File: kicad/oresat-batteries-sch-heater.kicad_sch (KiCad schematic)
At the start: 20 parts, among them Q20 PMV45EN, Q21 PMV45EN, Q38 PMV45EN, Q39 PMV45EN, Q42 MOSFET-PCH-SOT23-6, Q43 MOSFET-PCH-SOT23-6

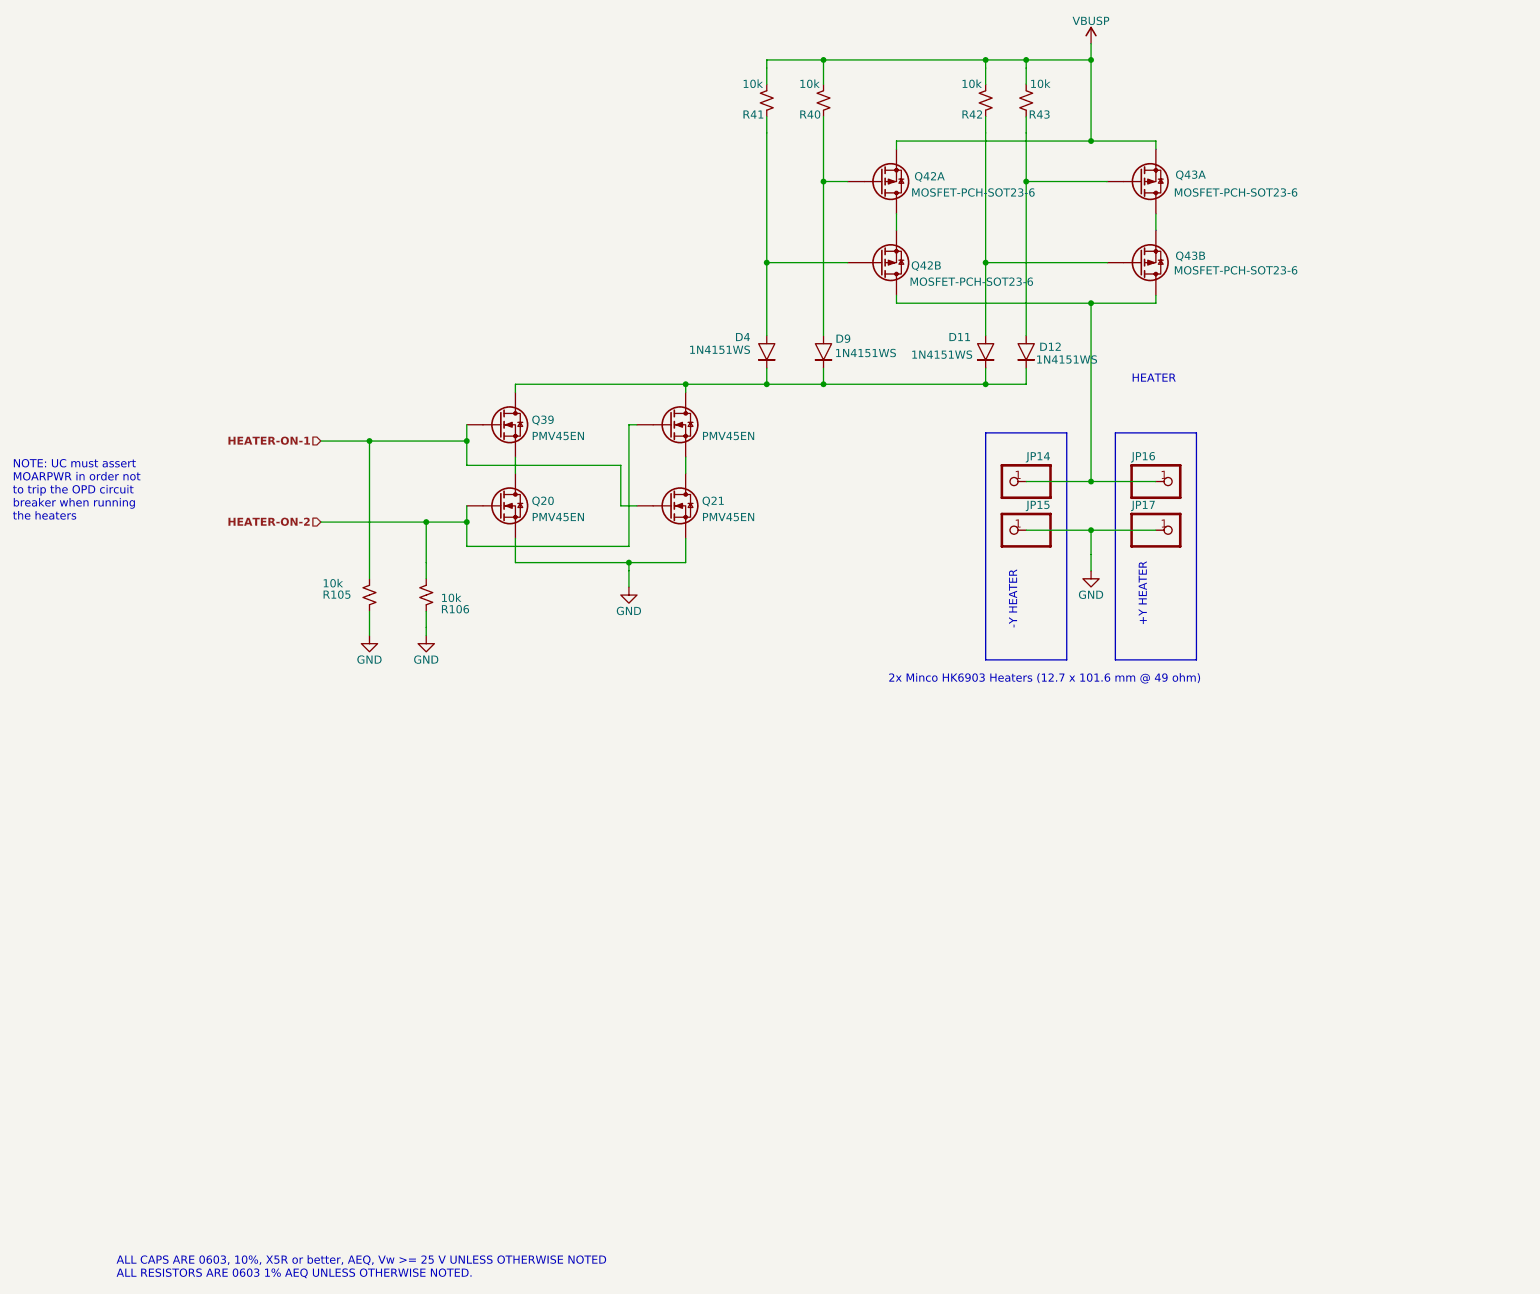
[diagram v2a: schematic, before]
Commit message: Progress on battery card v4
Moved in -batt cutoffs, which caused a lot of pain and suffering. Started updating BOM, and fixed all transistor packages. Updated resistor packages, too. Still needs a lot of cleanup, but probably 80% done now.
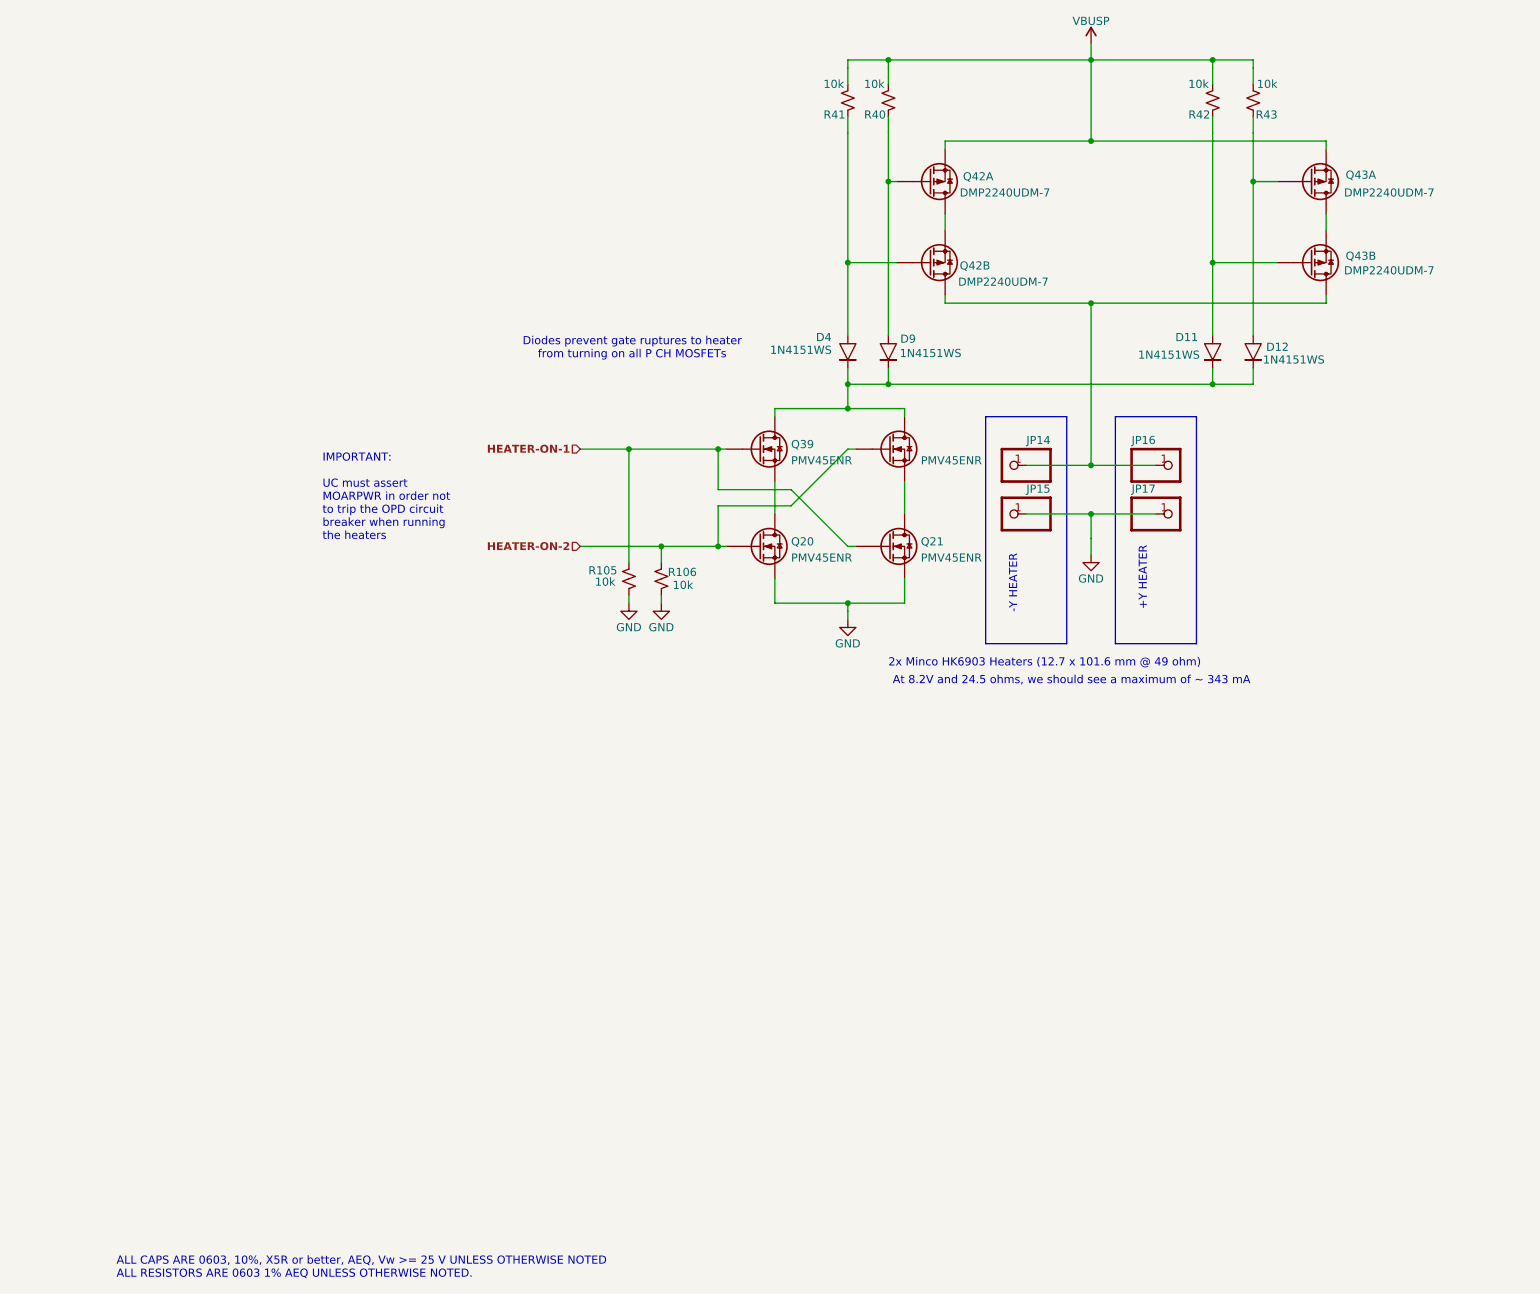
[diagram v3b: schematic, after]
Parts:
- Q20, Q21, Q38, Q39: value PMV45EN -> PMV45ENR; footprint oresat-batteries:SOT23-3 -> Package_TO_SOT_SMD:SOT-23; DIS (none) -> DigiKey; DPN (none) -> 1727-2307-1-ND; MFR (none) -> Nexperia; MPN (none) -> PMV45EN2R
- Q42, Q43: value MOSFET-PCH-SOT23-6 -> DMP2240UDM-7; footprint oresat-batteries:SOT23-6 -> Package_TO_SOT_SMD:SOT-23-6; DIS (none) -> DigiKey; DPN (none) -> DMP2240UDMDICT-ND; MFR (none) -> Diodes Incorporated; MPN (none) -> DMP2240UDM-7
- R105, R106, R40, R41, R42, R43: footprint oresat-batteries:.0603-C-NOSILK -> oresat-passives:0603-C-NOSILK
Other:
- note added: "At 8.2V and 24.5 ohms, we should see a maximum of ~ 343 mA"
- note added: "Diodes prevent gate ruptures to heater from turning on all P CH MOSFETs"
- note added: "IMPORTANT: UC must assert MOARPWR in order not to trip the OPD circuit breaker when running the heaters"
- note removed: "HEATER"
- note removed: "NOTE: UC must assert MOARPWR in order not to trip the OPD circuit breaker when running the heaters~{}"
- moved on the sheet: D11, D12, D4, D9, JP14, JP15, JP16, JP17, Q20, Q21, Q39, Q42A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

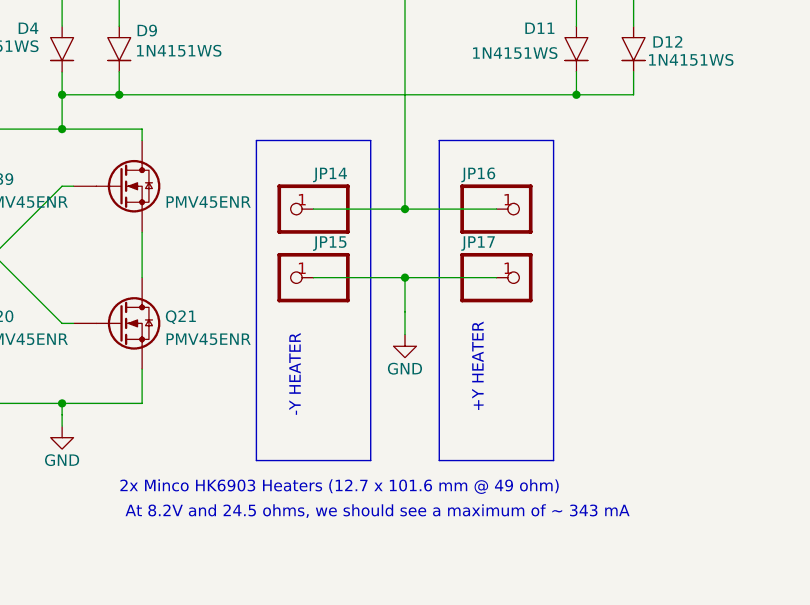
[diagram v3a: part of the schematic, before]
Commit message: Updated BOM, ready for polish and switch to MCXN
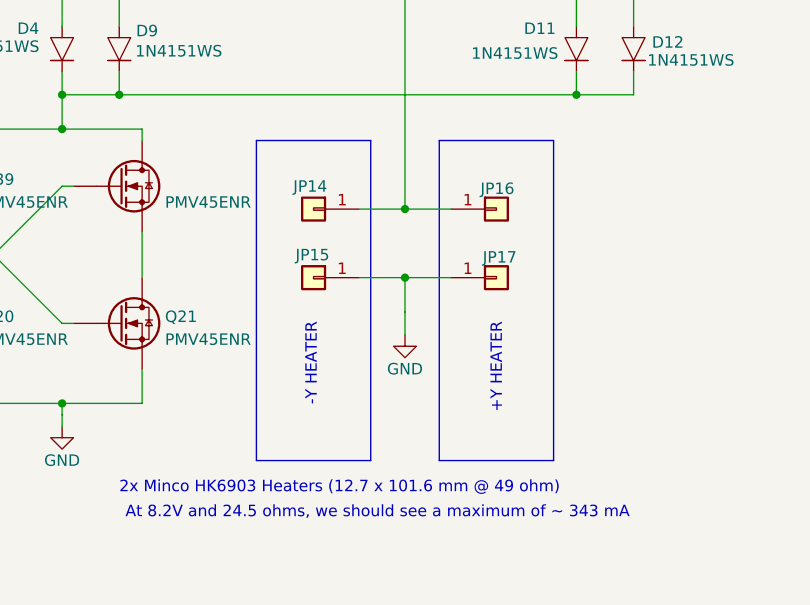
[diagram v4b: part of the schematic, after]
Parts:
- JP14, JP15, JP16, JP17: footprint oresat-batteries:1X01 -> Connector_PinHeader_2.54mm:PinHeader_1x01_P2.54mm_Vertical; symbol oresat-batteries-eagle-import:PINHD-1X1 -> Connector_Generic:Conn_01x01
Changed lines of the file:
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@@
 	(text "+Y HEATER"
 		(exclude_from_sim no)
-		(at 274.32 151.13 90)
+		(at 276.352 151.13 90)
 		(effects
 			(font
@@
 	(text "-Y HEATER"
 		(exclude_from_sim no)
-		(at 254 152.4 90)
+		(at 255.778 151.13 90)
 		(effects
 			(font
@@
 	(wire
 		(pts
-			(xy 255.27 146.05) (xy 265.43 146.05)
+			(xy 260.35 146.05) (xy 265.43 146.05)
 		)
 		(stroke
@@
 	(wire
 		(pts
-			(xy 255.27 138.43) (xy 265.43 138.43)
+			(xy 260.35 138.43) (xy 265.43 138.43)
 		)
 		(stroke
@@
 	(wire
 		(pts
-			(xy 265.43 138.43) (xy 275.59 138.43)
+			(xy 265.43 138.43) (xy 270.51 138.43)
 		)
 		(stroke
@@
 	(wire
 		(pts
-			(xy 265.43 146.05) (xy 275.59 146.05)
+			(xy 265.43 146.05) (xy 270.51 146.05)
 		)
 		(stroke
@@
 	)
 	(symbol
-		(lib_id "oresat-batteries-eagle-import:PINHD-1X1")
-		(at 278.13 146.05 0)
+		(lib_id "Connector_Generic:Conn_01x01")
+		(at 275.59 146.05 0)
 		(unit 1)
 		(exclude_from_sim no)
@@
 		(dnp no)
 		(property "Reference" "JP17"
-			(at 271.78 142.875 0)
+			(at 274.066 144.526 0)
 			(effects
 				(font
@@
 		)
 		(property "Value" "PINHD-1X1"
-			(at 271.78 151.13 0)
-			(effects
-				(font
-					(size 1.27 1.27)
-				)
-				(justify left bottom)
-				(hide yes)
-			)
-		)
-		(property "Footprint" "oresat-batteries:1X01"
-			(at 278.13 146.05 0)
-			(effects
-				(font
-					(size 1.27 1.27)
-				)
-				(hide yes)
-			)
-		)
-		(property "Datasheet" ""
-			(at 278.13 146.05 0)
-			(effects
-				(font
-					(size 1.27 1.27)
-				)
-				(hide yes)
-			)
-		)
-		(property "Description" ""
-			(at 278.13 146.05 0)
-			(effects
-				(font
-					(size 1.27 1.27)
-				)
+			(at 269.24 151.13 0)
+			(effects
+				(font
+					(size 1.27 1.27)
+				)
+				(justify left bottom)
+				(hide yes)
+			)
+		)
+		(property "Footprint" "Connector_PinHeader_2.54mm:PinHeader_1x01_P2.54mm_Vertical"
+			(at 275.59 146.05 0)
+			(effects
+				(font
+					(size 1.27 1.27)
+				)
+				(hide yes)
+			)
+		)
+		(property "Datasheet" "~"
+			(at 275.59 146.05 0)
+			(effects
+				(font
+					(size 1.27 1.27)
+				)
+				(hide yes)
+			)
+		)
+		(property "Description" "Generic connector, single row, 01x01, script generated (kicad-library-utils/schlib/autogen/connector/)"
+			(at 275.59 146.05 0)
+			(effects
+				(font
+					(size 1.27 1.27)
+				)
+				(hide yes)
 			)
 		)
@@
 	)
 	(symbol
-		(lib_id "oresat-batteries-eagle-import:PINHD-1X1")
-		(at 252.73 138.43 0)
+		(lib_id "Connector_Generic:Conn_01x01")
+		(at 255.27 138.43 0)
 		(mirror y)
 		(unit 1)
@@
 		(dnp no)
 		(property "Reference" "JP14"
-			(at 259.08 135.255 0)
+			(at 256.794 136.652 0)
 			(effects
 				(font
@@
 		)
 		(property "Value" "PINHD-1X1"
-			(at 259.08 143.51 0)
-			(effects
-				(font
-					(size 1.27 1.27)
-				)
-				(justify left bottom)
-				(hide yes)
-			)
-		)
-		(property "Footprint" "oresat-batteries:1X01"
-			(at 252.73 138.43 0)
-			(effects
-				(font
-					(size 1.27 1.27)
-				)
-				(hide yes)
-			)
-		)
-		(property "Datasheet" ""
-			(at 252.73 138.43 0)
-			(effects
-				(font
-					(size 1.27 1.27)
-				)
-				(hide yes)
-			)
-		)
-		(property "Description" ""
-			(at 252.73 138.43 0)
-			(effects
-				(font
-					(size 1.27 1.27)
-				)
+			(at 261.62 143.51 0)
+			(effects
+				(font
+					(size 1.27 1.27)
+				)
+				(justify left bottom)
+				(hide yes)
+			)
+		)
+		(property "Footprint" "Connector_PinHeader_2.54mm:PinHeader_1x01_P2.54mm_Vertical"
+			(at 255.27 138.43 0)
+			(effects
+				(font
+					(size 1.27 1.27)
+				)
+				(hide yes)
+			)
+		)
+		(property "Datasheet" "~"
+			(at 255.27 138.43 0)
+			(effects
+				(font
+					(size 1.27 1.27)
+				)
+				(hide yes)
+			)
+		)
+		(property "Description" "Generic connector, single row, 01x01, script generated (kicad-library-utils/schlib/autogen/connector/)"
+			(at 255.27 138.43 0)
+			(effects
+				(font
+					(size 1.27 1.27)
+				)
+				(hide yes)
 			)
 		)
@@
 	)
 	(symbol
-		(lib_id "oresat-batteries-eagle-import:PINHD-1X1")
-		(at 278.13 138.43 0)
+		(lib_id "Connector_Generic:Conn_01x01")
+		(at 275.59 138.43 0)
 		(unit 1)
 		(exclude_from_sim no)
@@
 		(dnp no)
 		(property "Reference" "JP16"
-			(at 271.78 135.255 0)
+			(at 273.812 136.906 0)
 			(effects
 				(font
@@
 		)
 		(property "Value" "PINHD-1X1"
-			(at 271.78 143.51 0)
-			(effects
-				(font
-					(size 1.27 1.27)
-				)
-				(justify left bottom)
-				(hide yes)
-			)
-		)
-		(property "Footprint" "oresat-batteries:1X01"
-			(at 278.13 138.43 0)
-			(effects
-				(font
-					(size 1.27 1.27)
-				)
-				(hide yes)
-			)
-		)
-		(property "Datasheet" ""
-			(at 278.13 138.43 0)
-			(effects
-				(font
-					(size 1.27 1.27)
-				)
-				(hide yes)
-			)
-		)
-		(property "Description" ""
-			(at 278.13 138.43 0)
-			(effects
-				(font
-					(size 1.27 1.27)
-				)
+			(at 269.24 143.51 0)
+			(effects
+				(font
+					(size 1.27 1.27)
+				)
+				(justify left bottom)
+				(hide yes)
+			)
+		)
+		(property "Footprint" "Connector_PinHeader_2.54mm:PinHeader_1x01_P2.54mm_Vertical"
+			(at 275.59 138.43 0)
+			(effects
+				(font
+					(size 1.27 1.27)
+				)
+				(hide yes)
+			)
+		)
+		(property "Datasheet" "~"
+			(at 275.59 138.43 0)
+			(effects
+				(font
+					(size 1.27 1.27)
+				)
+				(hide yes)
+			)
+		)
+		(property "Description" "Generic connector, single row, 01x01, script generated (kicad-library-utils/schlib/autogen/connector/)"
+			(at 275.59 138.43 0)
+			(effects
+				(font
+					(size 1.27 1.27)
+				)
+				(hide yes)
 			)
 		)
@@
 	)
 	(symbol
-		(lib_id "oresat-batteries-eagle-import:PINHD-1X1")
-		(at 252.73 146.05 0)
+		(lib_id "Connector_Generic:Conn_01x01")
+		(at 255.27 146.05 0)
 		(mirror y)
 		(unit 1)
@@
 		(dnp no)
 		(property "Reference" "JP15"
-			(at 259.08 142.875 0)
+			(at 257.048 144.272 0)
 			(effects
 				(font
@@
 		)
 		(property "Value" "PINHD-1X1"
-			(at 259.08 151.13 0)
-			(effects
-				(font
-					(size 1.27 1.27)
-				)
-				(justify left bottom)
-				(hide yes)
-			)
-		)
-		(property "Footprint" "oresat-batteries:1X01"
-			(at 252.73 146.05 0)
-			(effects
-				(font
-					(size 1.27 1.27)
-				)
-				(hide yes)
-			)
-		)
-		(property "Datasheet" ""
-			(at 252.73 146.05 0)
-			(effects
-				(font
-					(size 1.27 1.27)
-				)
-				(hide yes)
-			)
-		)
-		(property "Description" ""
-			(at 252.73 146.05 0)
-			(effects
-				(font
-					(size 1.27 1.27)
-				)
-			)
-		)
+			(at 261.62 151.13 0)
+			(effects
+				(font
+					(size 1.27 1.27)
+				)
+				(justify left bottom)
+				(hide yes)
+			)
+		)
+		(property "Footprint" "Connector_PinHeader_2.54mm:PinHeader_1x01_P2.54mm_Vertical"
+			(at 255.27 146.05 0)
+			(effects
+				(font
+					(size 1.27 1.27)
+				)
+				(hide yes)
+			)
+		)
+		(property "Datasheet" "~"
+			(at 255.27 146.05 0)
+			(effects
+				(font
+					(size 1.27 1.27)
+				)
+				(hide yes)
+			)
+		)
+		(property "Description" "Generic connector, single row, 01x01, script generated (kicad-library-utils/schlib/autogen/connector/)"
+			(at 255.27 146.05 0)
+			(effects
+				(font
+					(size 1.27 1.27)
+				)
+				(hide yes)
+			)
+		)

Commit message: Not sure what changed from back in February, but committing anyway :)
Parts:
- added R100, R99: HK6903, symbol Device:Heater
- D11, D12, D4, D9: DIS (none) -> DigiKey; DPN (none) -> 112-1N4151WS-E3-08CT-ND; MFR (none) -> Vishay; MPN (none) -> 1N4151WS-E3-08
- JP14, JP15, JP16, JP17: DIS (none) -> N/A; DPN (none) -> N/A; MFR (none) -> N/A; MPN (none) -> N/A; now left out of the parts list
- R105, R106, R40, R41, R42, R43: DIS Digi-Key -> DigiKey; DPN 311-10.0KHRCT-ND -> RMCF0603FT10K0CT-ND; MFR Yageo -> Stackpole Electronics; MPN RC0603FR-0710KL -> RMCF0603FT10K0
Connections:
- no-connect marks 0 -> 4
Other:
- moved on the sheet: D11, D12, JP14, JP15, JP16, JP17, Q43A, Q43B, R42, R43

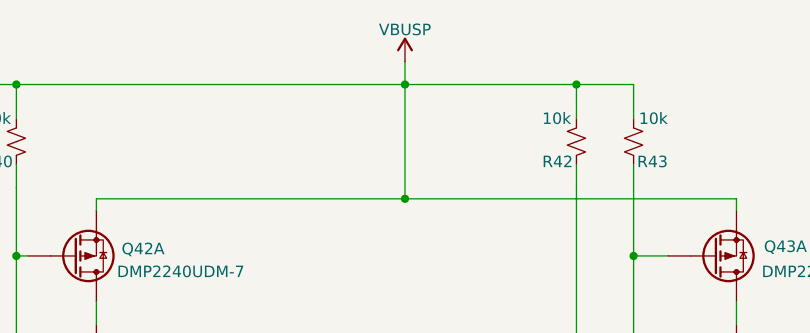
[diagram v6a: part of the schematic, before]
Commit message: Added MCXN. Preliminary power layout, started removal of old symbols and footprints.
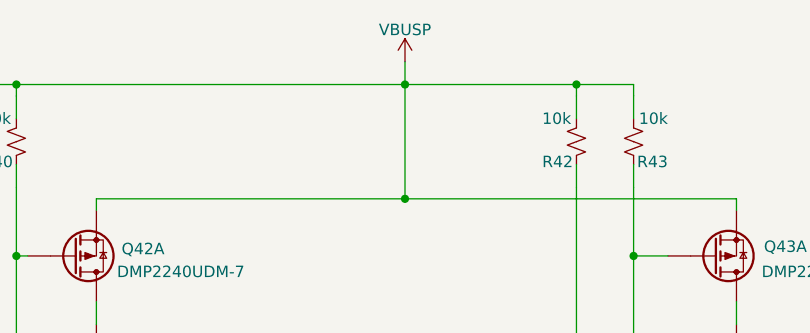
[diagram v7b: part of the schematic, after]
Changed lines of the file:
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@@
 	)
 	(symbol
-		(lib_id "oresat-batteries-eagle-import:VBUSP")
+		(lib_id "oresat-power:VBUSP")
 		(at 276.86 72.39 0)
 		(unit 1)
@@
 			)
 		)
-		(property "Description" ""
+		(property "Description" "Power symbol creates a global label with name \"VBUSP\""
 			(at 276.86 72.39 0)
 			(effects
@@
 					(size 1.27 1.27)
 				)
+				(hide yes)
 			)
 		)
